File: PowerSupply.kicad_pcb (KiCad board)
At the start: 2 copper layers, 8 parts, among them J1 Screw_Terminal, J2 Screw_Terminal, U1 L7805, U2 LD1117S33TR

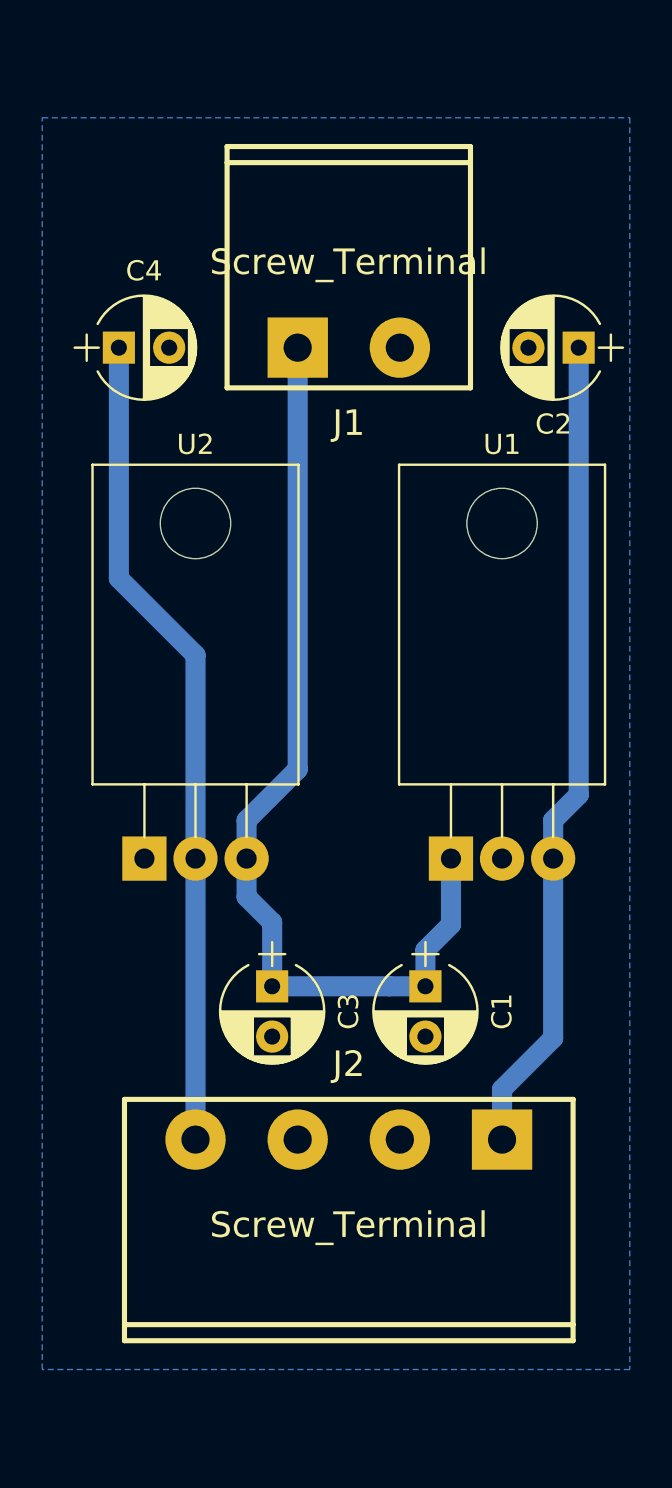
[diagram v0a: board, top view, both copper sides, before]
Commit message: Added printable parts
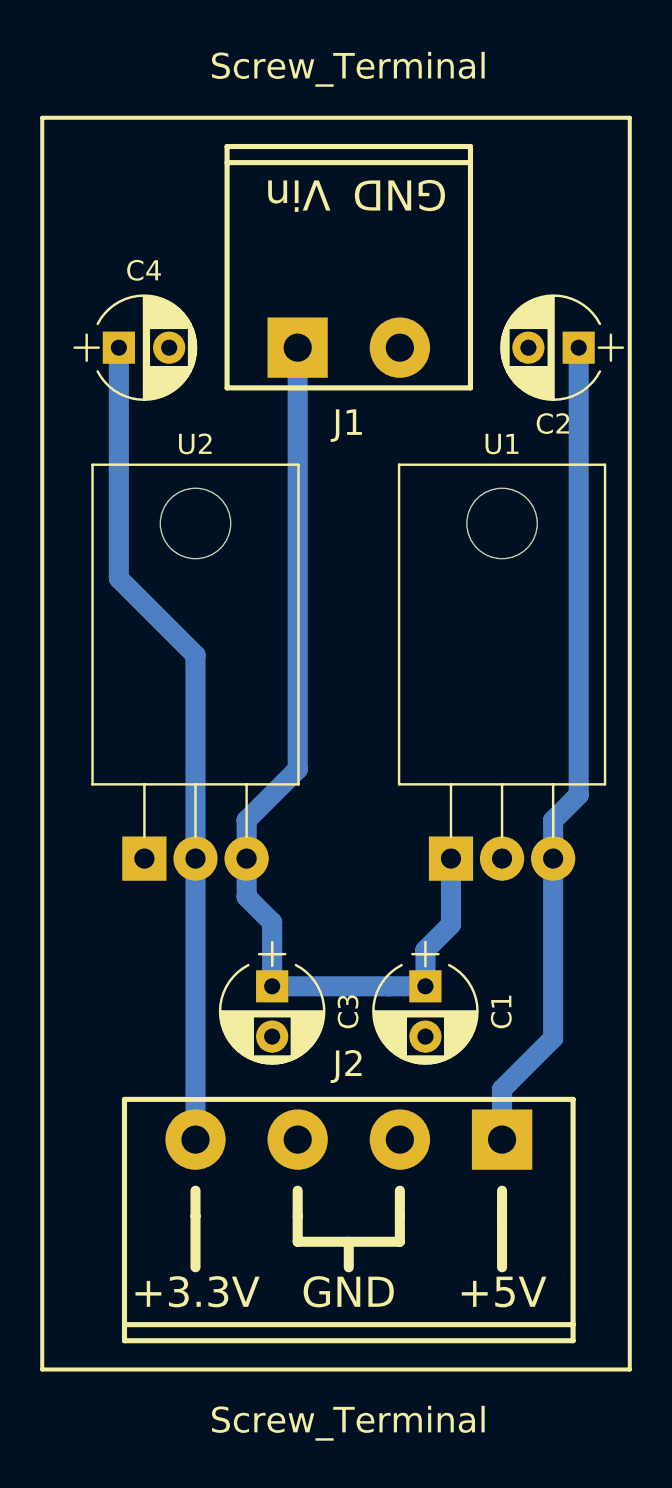
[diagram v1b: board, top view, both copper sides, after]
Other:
- board text added: "+3.3V"
- board text added: "+5V"
- board text added: "GND"
- board text added: "Vin"
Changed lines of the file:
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@@
     (links 16)
     (no_connects 0)
-    (area 165.1 67.31 194.330001 129.540001)
+    (area 164.999999 63.2508 194.410001 133.7516)
     (thickness 1.6)
-    (drawings 0)
+    (drawings 19)
     (tracks 21)
     (zones 0)
@@
     (pad_to_mask_clearance 0.2)
     (aux_axis_origin 0 0)
-    (visible_elements FFFFFF7F)
+    (visible_elements 7FFFFFFF)
     (pcbplotparams
       (layerselection 0x00000_80000000)
@@
     (add_net GNDD)
     (add_net VCC)
+  )
+  (module w_conn_screw:mstba_2,5%2f4-g-5,08 (layer F.Cu)
+    (at 180.34 118.11 180)
+    (descr "Terminal block 2 pins, Phoenix MSTBA 2,5/4-G-5,08")
+    (fp_text reference J2 (at 0 3.74904 180) (layer F.SilkS)
+      (effects (font (thickness 0.3048)))
+    )
+    (fp_text value Screw_Terminal (at 0 -13.97 180) (layer F.SilkS)
+      (effects (font (thickness 0.3048)))
+    )
+    (fp_line (start 11.1506 -9.99998) (end -11.1506 -9.99998) (layer F.SilkS) (width 0.254))
+    (fp_line (start -11.1506 -9.19988) (end 11.1506 -9.19988) (layer F.SilkS) (width 0.254))
+    (fp_line (start -11.1506 1.99898) (end 11.1506 1.99898) (layer F.SilkS) (width 0.254))
+    (fp_line (start -11.1506 1.99898) (end -11.1506 -9.99998) (layer F.SilkS) (width 0.254))
+    (fp_line (start 11.1506 1.99898) (end 11.1506 -9.99998) (layer F.SilkS) (width 0.254))
+    (pad 1 thru_hole rect (at -7.62 0 180) (size 2.99974 2.99974) (drill 1.39954) (layers *.Cu *.Mask F.SilkS)
+      (net 3 +5V))
+    (pad 2 thru_hole circle (at -2.54 0 180) (size 2.99974 2.99974) (drill 1.39954) (layers *.Cu *.Mask F.SilkS)
+      (net 2 GNDD))
+    (pad 4 thru_hole circle (at 7.62 0 180) (size 2.99974 2.99974) (drill 1.39954) (layers *.Cu *.Mask F.SilkS)
+      (net 4 +3V3))
+    (pad 3 thru_hole circle (at 2.54 0 180) (size 2.99974 2.99974) (drill 1.39954) (layers *.Cu *.Mask F.SilkS)
+      (net 2 GNDD))
+    (model walter/conn_screw/mstba_2,5-4-g-5,08.wrl
+      (at (xyz 0 0 0))
+      (scale (xyz 1 1 1))
+      (rotate (xyz 0 0 0))
+    )
   )
   (module Capacitors_THT:CP_Radial_D5.0mm_P2.50mm (layer F.Cu)
@@
       (effects (font (thickness 0.3048)))
     )
-    (fp_text value Screw_Terminal (at 0 -4.24942) (layer F.SilkS)
+    (fp_text value Screw_Terminal (at 0 -13.97) (layer F.SilkS)
       (effects (font (thickness 0.3048)))
     )
@@
       (net 2 GNDD))
     (model walter/conn_screw/mstba_2,5-2-g-5,08.wrl
-      (at (xyz 0 0 0))
-      (scale (xyz 1 1 1))
-      (rotate (xyz 0 0 0))
-    )
-  )
-  (module w_conn_screw:mstba_2,5%2f4-g-5,08 (layer F.Cu)
-    (at 180.34 118.11 180)
-    (descr "Terminal block 2 pins, Phoenix MSTBA 2,5/4-G-5,08")
-    (fp_text reference J2 (at 0 3.74904 180) (layer F.SilkS)
-      (effects (font (thickness 0.3048)))
-    )
-    (fp_text value Screw_Terminal (at 0 -4.24942 180) (layer F.SilkS)
-      (effects (font (thickness 0.3048)))
-    )
-    (fp_line (start 11.1506 -9.99998) (end -11.1506 -9.99998) (layer F.SilkS) (width 0.254))
-    (fp_line (start -11.1506 -9.19988) (end 11.1506 -9.19988) (layer F.SilkS) (width 0.254))
-    (fp_line (start -11.1506 1.99898) (end 11.1506 1.99898) (layer F.SilkS) (width 0.254))
-    (fp_line (start -11.1506 1.99898) (end -11.1506 -9.99998) (layer F.SilkS) (width 0.254))
-    (fp_line (start 11.1506 1.99898) (end 11.1506 -9.99998) (layer F.SilkS) (width 0.254))
-    (pad 1 thru_hole rect (at -7.62 0 180) (size 2.99974 2.99974) (drill 1.39954) (layers *.Cu *.Mask F.SilkS)
-      (net 3 +5V))
-    (pad 2 thru_hole circle (at -2.54 0 180) (size 2.99974 2.99974) (drill 1.39954) (layers *.Cu *.Mask F.SilkS)
-      (net 2 GNDD))
-    (pad 4 thru_hole circle (at 7.62 0 180) (size 2.99974 2.99974) (drill 1.39954) (layers *.Cu *.Mask F.SilkS)
-      (net 4 +3V3))
-    (pad 3 thru_hole circle (at 2.54 0 180) (size 2.99974 2.99974) (drill 1.39954) (layers *.Cu *.Mask F.SilkS)
-      (net 2 GNDD))
-    (model walter/conn_screw/mstba_2,5-4-g-5,08.wrl
       (at (xyz 0 0 0))
       (scale (xyz 1 1 1))
@@
     )
   )
+  (gr_line (start 180.34 123.19) (end 180.34 124.46) (angle 90) (layer F.SilkS) (width 0.5))
+  (gr_line (start 182.88 123.19) (end 182.88 121.92) (angle 90) (layer F.SilkS) (width 0.5))
+  (gr_line (start 177.8 123.19) (end 182.88 123.19) (angle 90) (layer F.SilkS) (width 0.5))
+  (gr_line (start 177.8 121.92) (end 177.8 123.19) (angle 90) (layer F.SilkS) (width 0.5))
+  (gr_line (start 172.72 121.92) (end 172.72 124.46) (angle 90) (layer F.SilkS) (width 0.5))
+  (gr_line (start 187.96 121.92) (end 187.96 124.46) (angle 90) (layer F.SilkS) (width 0.5))
+  (gr_text Vin (at 177.8 71.12 180) (layer F.SilkS)
+    (effects (font (size 1.5 1.5) (thickness 0.375)))
+  )
+  (gr_text GND (at 182.88 71.12 180) (layer F.SilkS)
+    (effects (font (size 1.5 1.5) (thickness 0.375)))
+  )
+  (gr_line (start 187.96 120.65) (end 187.96 121.92) (angle 90) (layer F.SilkS) (width 0.5))
+  (gr_line (start 172.72 120.65) (end 172.72 121.92) (angle 90) (layer F.SilkS) (width 0.5))
+  (gr_line (start 182.88 121.92) (end 182.88 120.65) (angle 90) (layer F.SilkS) (width 0.5))
+  (gr_line (start 177.8 120.65) (end 177.8 121.92) (angle 90) (layer F.SilkS) (width 0.5))
+  (gr_text GND (at 180.34 125.73) (layer F.SilkS)
+    (effects (font (size 1.5 1.5) (thickness 0.375)))
+  )
+  (gr_text +3.3V (at 172.72 125.73) (layer F.SilkS)
+    (effects (font (size 1.5 1.5) (thickness 0.375)))
+  )
+  (gr_text +5V (at 187.96 125.73) (layer F.SilkS)
+    (effects (font (size 1.5 1.5) (thickness 0.375)))
+  )
+  (gr_line (start 165.1 67.31) (end 165.1 129.54) (angle 90) (layer F.SilkS) (width 0.2))
+  (gr_line (start 194.31 67.31) (end 165.1 67.31) (angle 90) (layer F.SilkS) (width 0.2))
+  (gr_line (start 194.31 129.54) (end 194.31 67.31) (angle 90) (layer F.SilkS) (width 0.2))
+  (gr_line (start 165.1 129.54) (end 194.31 129.54) (angle 90) (layer F.SilkS) (width 0.2))
   (segment (start 175.26 104.14) (end 175.26 106.04) (width 1) (layer B.Cu) (net 1))
   (segment (start 177.8 99.7) (end 175.26 102.24) (width 1) (layer B.Cu) (net 1))
